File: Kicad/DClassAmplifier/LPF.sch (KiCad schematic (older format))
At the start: 15 parts, among them J5 Conn_01x02, J6 Conn_01x02, U3 AD8567ARUZ

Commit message: Update Terminal Block Footprints
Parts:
- J5, J6: footprint Connector_PinSocket_2.54mm:PinSocket_1x02_P2.54mm_Vertical -> TerminalBlock:TerminalBlock_bornier-2_P5.08mm
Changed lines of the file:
@@
 F 0 "J6" H 1530 3942 50  0000 L CNN
 F 1 "Conn_01x02" H 1530 3851 50  0000 L CNN
-F 2 "Connector_PinSocket_2.54mm:PinSocket_1x02_P2.54mm_Vertical" H 1450 3950 50  0001 C CNN
+F 2 "TerminalBlock:TerminalBlock_bornier-2_P5.08mm" H 1450 3950 50  0001 C CNN
 F 3 "~" H 1450 3950 50  0001 C CNN
 	1    1450 3950
@@
 F 0 "J5" H 1530 3342 50  0000 L CNN
 F 1 "Conn_01x02" H 1530 3251 50  0000 L CNN
-F 2 "Connector_PinSocket_2.54mm:PinSocket_1x02_P2.54mm_Vertical" H 1450 3350 50  0001 C CNN
+F 2 "TerminalBlock:TerminalBlock_bornier-2_P5.08mm" H 1450 3350 50  0001 C CNN
 F 3 "~" H 1450 3350 50  0001 C CNN
 	1    1450 3350

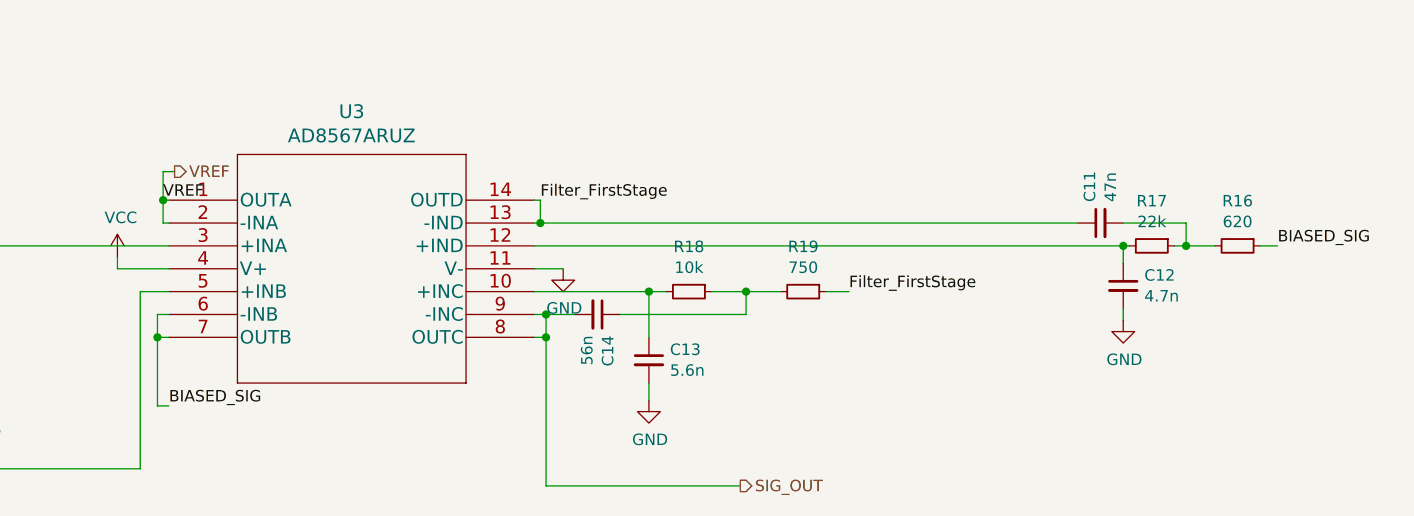
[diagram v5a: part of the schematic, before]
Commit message: Add Test Points
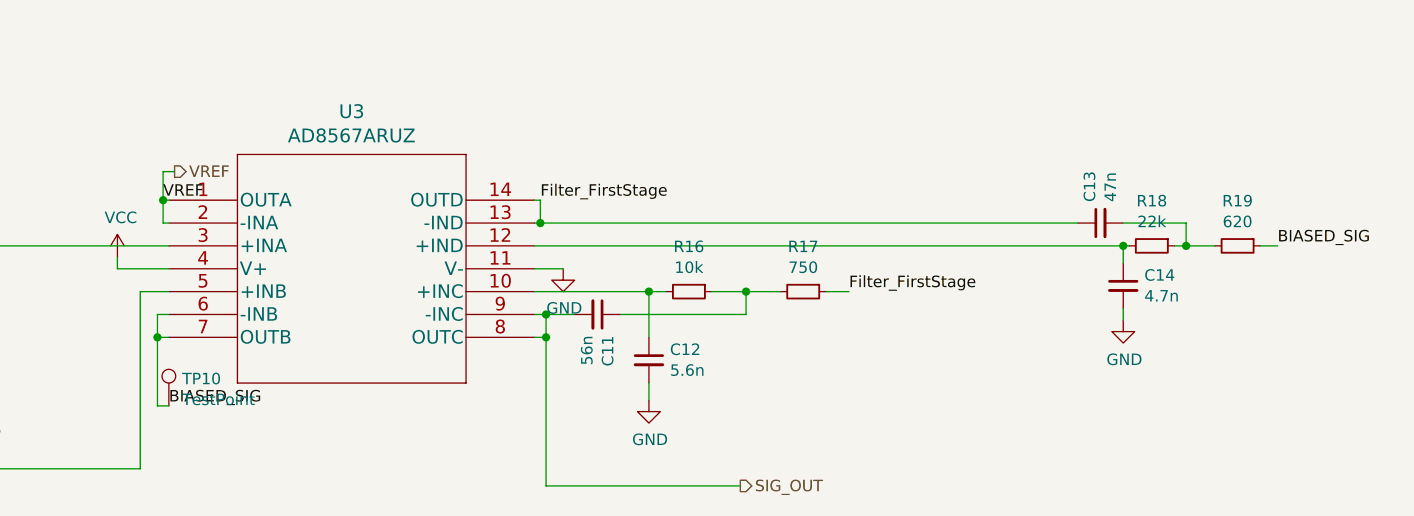
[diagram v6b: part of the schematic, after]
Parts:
- added TP10: TestPoint, TestPoint:TestPoint_Pad_D2.0mm, symbol Connector:TestPoint
- renumbered C14 to C11, C13 to C12, C11 to C13, C12 to C14, R18 to R16, R19 to R17, R17 to R18, R16 to R19
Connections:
- net BIASED_SIG: now also TP10.1
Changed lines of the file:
@@
 $EndDescr
 $Comp
-L Device:R_Small R17
+L Device:R_Small R18
 U 1 1 6119FD9F
 P 9925 5025
-F 0 "R17" V 9729 5025 50  0000 C CNN
+F 0 "R18" V 9729 5025 50  0000 C CNN
 F 1 "22k" V 9820 5025 50  0000 C CNN
 F 2 "Resistor_SMD:R_0603_1608Metric_Pad0.98x0.95mm_HandSolder" H 9925 5025 50  0001 C CNN
@@
 $EndComp
 $Comp
-L Device:R_Small R16
+L Device:R_Small R19
 U 1 1 611A0CB6
 P 10300 5025
-F 0 "R16" V 10104 5025 50  0000 C CNN
+F 0 "R19" V 10104 5025 50  0000 C CNN
 F 1 "620" V 10195 5025 50  0000 C CNN
 F 2 "Resistor_SMD:R_0603_1608Metric_Pad0.98x0.95mm_HandSolder" H 10300 5025 50  0001 C CNN
@@
 $EndComp
 $Comp
-L Device:C_Small C12
+L Device:C_Small C14
 U 1 1 611A751B
 P 9800 5200
-F 0 "C12" H 9892 5246 50  0000 L CNN
+F 0 "C14" H 9892 5246 50  0000 L CNN
 F 1 "4.7n" H 9892 5155 50  0000 L CNN
 F 2 "Capacitor_SMD:C_0603_1608Metric_Pad1.08x0.95mm_HandSolder" H 9800 5200 50  0001 C CNN
@@
 	9800 5300 9800 5350
 $Comp
-L power:GND #PWR0143
+L power:GND #PWR043
 U 1 1 611AAC29
 P 9800 5350
-F 0 "#PWR0143" H 9800 5100 50  0001 C CNN
+F 0 "#PWR043" H 9800 5100 50  0001 C CNN
 F 1 "GND" H 9805 5177 50  0000 C CNN
 F 2 "" H 9800 5350 50  0001 C CNN
@@
 $EndComp
 $Comp
-L Device:C_Small C13
+L Device:C_Small C12
 U 1 1 611BBE57
 P 7725 5525
-F 0 "C13" H 7817 5571 50  0000 L CNN
+F 0 "C12" H 7817 5571 50  0000 L CNN
 F 1 "5.6n" H 7817 5480 50  0000 L CNN
 F 2 "Capacitor_SMD:C_0603_1608Metric_Pad1.08x0.95mm_HandSolder" H 7725 5525 50  0001 C CNN
@@
 $EndComp
 $Comp
-L Device:R_Small R18
+L Device:R_Small R16
 U 1 1 611BC850
 P 7900 5225
-F 0 "R18" V 7704 5225 50  0000 C CNN
+F 0 "R16" V 7704 5225 50  0000 C CNN
 F 1 "10k" V 7795 5225 50  0000 C CNN
 F 2 "Resistor_SMD:R_0603_1608Metric_Pad0.98x0.95mm_HandSolder" H 7900 5225 50  0001 C CNN
@@
 $EndComp
 $Comp
-L Device:R_Small R19
+L Device:R_Small R17
 U 1 1 611BD0E0
 P 8400 5225
-F 0 "R19" V 8204 5225 50  0000 C CNN
+F 0 "R17" V 8204 5225 50  0000 C CNN
 F 1 "750" V 8295 5225 50  0000 C CNN
 F 2 "Resistor_SMD:R_0603_1608Metric_Pad0.98x0.95mm_HandSolder" H 8400 5225 50  0001 C CNN
@@
 	8600 5225 8500 5225
 $Comp
-L Device:C_Small C14
+L Device:C_Small C11
 U 1 1 611C0153
 P 7500 5325
-F 0 "C14" H 7592 5371 50  0000 L CNN
+F 0 "C11" H 7592 5371 50  0000 L CNN
 F 1 "56n" H 7592 5280 50  0000 L CNN
 F 2 "Capacitor_SMD:C_0603_1608Metric_Pad1.08x0.95mm_HandSolder" H 7500 5325 50  0001 C CNN
@@
 $EndComp
 $Comp
-L power:GND #PWR0144
+L power:GND #PWR042
 U 1 1 611C31DE
 P 7725 5700
-F 0 "#PWR0144" H 7725 5450 50  0001 C CNN
+F 0 "#PWR042" H 7725 5450 50  0001 C CNN
 F 1 "GND" H 7730 5527 50  0000 C CNN
 F 2 "" H 7725 5700 50  0001 C CNN
@@
 $EndComp
 $Comp
-L power:VCC #PWR0134
+L power:VCC #PWR040
 U 1 1 61106B01
 P 5400 5075
-AR Path="/610C616D/61106B01" Ref="#PWR0134"  Part="1"
+AR Path="/610C616D/61106B01" Ref="#PWR040"  Part="1"
 AR Path="/611D4178/61106B01" Ref="#PWR?"  Part="1"
-F 0 "#PWR0134" H 5400 4925 50  0001 C CNN
+F 0 "#PWR040" H 5400 4925 50  0001 C CNN
 F 1 "VCC" H 5415 5248 50  0000 C CNN
 F 2 "" H 5400 5075 50  0001 C CNN
@@
 $EndComp
 $Comp
-L power:GND #PWR0135
+L power:GND #PWR041
 U 1 1 61106B09
 P 7350 5125
-AR Path="/610C616D/61106B09" Ref="#PWR0135"  Part="1"
+AR Path="/610C616D/61106B09" Ref="#PWR041"  Part="1"
 AR Path="/611D4178/61106B09" Ref="#PWR?"  Part="1"
-F 0 "#PWR0135" H 7350 4875 50  0001 C CNN
+F 0 "#PWR041" H 7350 4875 50  0001 C CNN
 F 1 "GND" H 7355 4952 50  0000 C CNN
 F 2 "" H 7350 5125 50  0001 C CNN
@@
 P 4425 5375
 AR Path="/611D4178/61106B3C" Ref="#PWR?"  Part="1"
-AR Path="/610C616D/61106B3C" Ref="#PWR0136"  Part="1"
-F 0 "#PWR0136" H 4425 5125 50  0001 C CNN
+AR Path="/610C616D/61106B3C" Ref="#PWR039"  Part="1"
+F 0 "#PWR039" H 4425 5125 50  0001 C CNN
 F 1 "GND" H 4430 5202 50  0000 C CNN
 F 2 "" H 4425 5375 50  0001 C CNN
@@
 P 4425 4675
 AR Path="/611D4178/61106B43" Ref="#PWR?"  Part="1"
-AR Path="/610C616D/61106B43" Ref="#PWR0137"  Part="1"
-F 0 "#PWR0137" H 4425 4525 50  0001 C CNN
+AR Path="/610C616D/61106B43" Ref="#PWR038"  Part="1"
+F 0 "#PWR038" H 4425 4525 50  0001 C CNN
 F 1 "VCC" H 4440 4848 50  0000 C CNN
 F 2 "" H 4425 4675 50  0001 C CNN
@@
 P 1250 4050
 AR Path="/611D4178/61106B56" Ref="#PWR?"  Part="1"
-AR Path="/610C616D/61106B56" Ref="#PWR0138"  Part="1"
-F 0 "#PWR0138" H 1250 3800 50  0001 C CNN
+AR Path="/610C616D/61106B56" Ref="#PWR037"  Part="1"
+F 0 "#PWR037" H 1250 3800 50  0001 C CNN
 F 1 "GND" H 1255 3877 50  0000 C CNN
 F 2 "" H 1250 4050 50  0001 C CNN
@@
 P 1250 3950
 AR Path="/611D4178/61106B5C" Ref="#PWR?"  Part="1"
-AR Path="/610C616D/61106B5C" Ref="#PWR0139"  Part="1"
-F 0 "#PWR0139" H 1250 3800 50  0001 C CNN
+AR Path="/610C616D/61106B5C" Ref="#PWR036"  Part="1"
+F 0 "#PWR036" H 1250 3800 50  0001 C CNN
 F 1 "VCC" H 1265 4123 50  0000 C CNN
 F 2 "" H 1250 3950 50  0001 C CNN
@@
 P 1250 3450
 AR Path="/611D4178/61106B68" Ref="#PWR?"  Part="1"
-AR Path="/610C616D/61106B68" Ref="#PWR0140"  Part="1"
-F 0 "#PWR0140" H 1250 3200 50  0001 C CNN
+AR Path="/610C616D/61106B68" Ref="#PWR035"  Part="1"
+F 0 "#PWR035" H 1250 3200 50  0001 C CNN
 F 1 "GND" H 1255 3277 50  0000 C CNN
 F 2 "" H 1250 3450 50  0001 C CNN
@@
 	4700 5725 4700 5775
 Wire Wire Line
-	4700 6000 5500 6000
-Wire Wire Line
 	5500 6000 5500 5225
 Wire Wire Line
@@
 	7250 4825 7225 4825
 $Comp
-L Device:C_Small C11
+L Device:C_Small C13
 U 1 1 611A7CBC
 P 9700 4925
-F 0 "C11" H 9792 4971 50  0000 L CNN
+F 0 "C13" H 9792 4971 50  0000 L CNN
 F 1 "47n" H 9792 4880 50  0000 L CNN
 F 2 "Capacitor_SMD:C_0603_1608Metric_Pad1.08x0.95mm_HandSolder" H 9700 4925 50  0001 C CNN
@@
 	7275 6075 8125 6075
 Connection ~ 7275 5425
+Wire Wire Line
+	4700 6000 5500 6000
+$Comp
+L Connector:TestPoint TP?
+U 1 1 6110E8F0
+P 5625 5725
+AR Path="/6110E8F0" Ref="TP?"  Part="1"
+AR Path="/610C616D/6110E8F0" Ref="TP10"  Part="1"
+F 0 "TP10" H 5683 5843 50  0000 L CNN
+F 1 "TestPoint" H 5683 5752 50  0000 L CNN
+F 2 "TestPoint:TestPoint_Pad_D2.0mm" H 5825 5725 50  0001 C CNN
+F 3 "~" H 5825 5725 50  0001 C CNN
+	1    5625 5725
+	1    0    0    -1
+$EndComp
 $EndSCHEMATC

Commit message: Load Components into PCBDOC
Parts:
- U3: footprint RU_14_ADI -> AD8567ARUZ:AD8567ARUZ
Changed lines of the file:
@@
 F 0 "U3" H 6425 5212 60  0000 C CNN
 F 1 "AD8567ARUZ" H 6425 5106 60  0000 C CNN
-F 2 "RU_14_ADI" H 6425 5065 60  0001 C CNN
+F 2 "AD8567ARUZ:AD8567ARUZ" H 6425 5065 60  0001 C CNN
 F 3 "" H 5625 4825 60  0000 C CNN
 	1    5625 4825

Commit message: Added input to global schematic
Changed the sig_in net label in the LPF sheet to a hierarchical net label of the same name
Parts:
- U3: symbol AD8567ARUZ:AD8567ARUZ -> DClassAmplifier-rescue:AD8567ARUZ-AD8567ARUZ
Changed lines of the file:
@@
 $Descr A4 11693 8268
 encoding utf-8
-Sheet 6 6
+Sheet 2 6
 Title ""
 Date ""
@@
 SIG_OUT
 $Comp
-L AD8567ARUZ:AD8567ARUZ U3
+L DClassAmplifier-rescue:AD8567ARUZ-AD8567ARUZ U3
 U 1 1 61100E74
 P 5625 4825
+AR Path="/61100E74" Ref="U3"  Part="1"
+AR Path="/610C616D/61100E74" Ref="U3"  Part="1"
 F 0 "U3" H 6425 5212 60  0000 C CNN
 F 1 "AD8567ARUZ" H 6425 5106 60  0000 C CNN
@@
 Text Label 1250 3350 2    50   ~ 0
 SIG_IN
-Text Label 4375 6000 2    50   ~ 0
-SIG_IN
 Text Label 5600 4825 0    50   ~ 0
 VREF
@@
 	1    0    0    -1
 $EndComp
+Wire Wire Line
+	4400 6000 4375 6000
+Text HLabel 4400 6000 0    50   Input ~ 0
+SIG_IN
 $EndSCHEMATC
